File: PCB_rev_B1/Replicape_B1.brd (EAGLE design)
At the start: 107.3 x 69.5 mm, 234 parts, among them IC1 TMC2100-LA, IC10 74AHC1G126DCK, IC11 74AHC1G126DCK, IC12 TMC2100-LA, IC13 74AHC1G126DCK, IC14 74AHC1G126DCK, IC15 TMC2100-LA, IC16 74AHC1G126DCK, IC17 74AHC1G126DCK, IC2 TMC2100-LA, IC3 74AHC1G126DCK, IC4 74AHC1G126DCK, IC5 TMC2100-LA, IC6 74AHC1G126DCK, IC7 74AHC1G126DCK, IC8 74AHC1G126DCK, IC9 74AHC1G126DCK, P8 F-2X23-, P9 F-2X23-, Q1 AON6758, Q2 AON6758, Q3 AON6758, U1 SN74AHC595PW, U10 RT8268, U11 PCA9685PW, U18 CAT24C256, U19 CD4050BD, U2 SN74AHC595PW, U3 SN74AHC595PW, U4 SN74AHC595PW, U5 SN74AHC595PW, U6 MCP16321, X1 22-05-7038-03, X10 22-05-7038-03, X11 22-05-7028-02, X12 22-05-7048-04, X13 22-05-7038-03, X14 22-05-7048-04, X15 22-05-7048-04, X16 22-05-7048-04, X17 22-05-7048-04, X18 22-05-7048-04, X19 22-05-7038-03, X2 MSTBA4, X20 MSTBA4, X21 MSTBA2, X22 22-05-7038-03, X23 22-05-7038-03, X3 MSTBA2, X4 22-05-7028-02, X5 22-05-7028-02, X6 22-05-7028-02, X7 22-05-7028-02, X8 22-05-7028-02, X9 22-05-7028-02

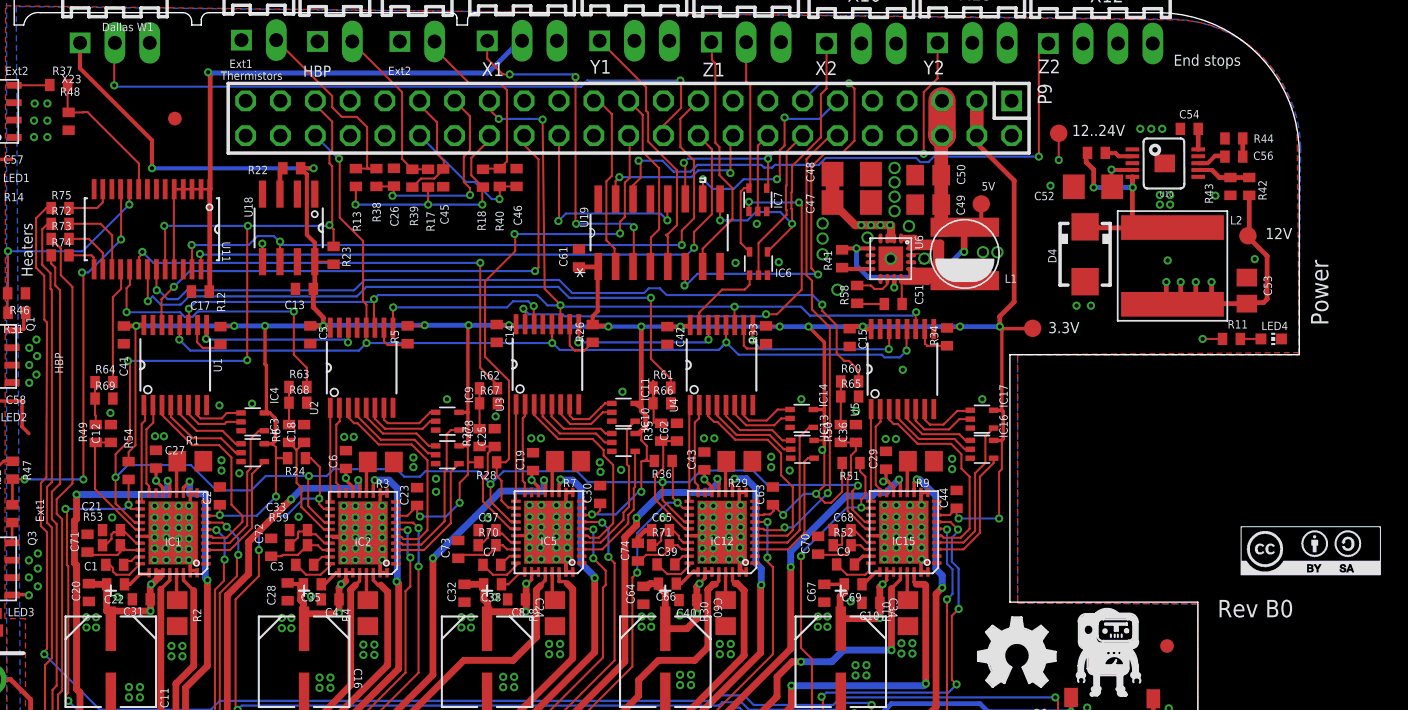
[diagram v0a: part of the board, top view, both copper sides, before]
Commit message: Fixed thermals
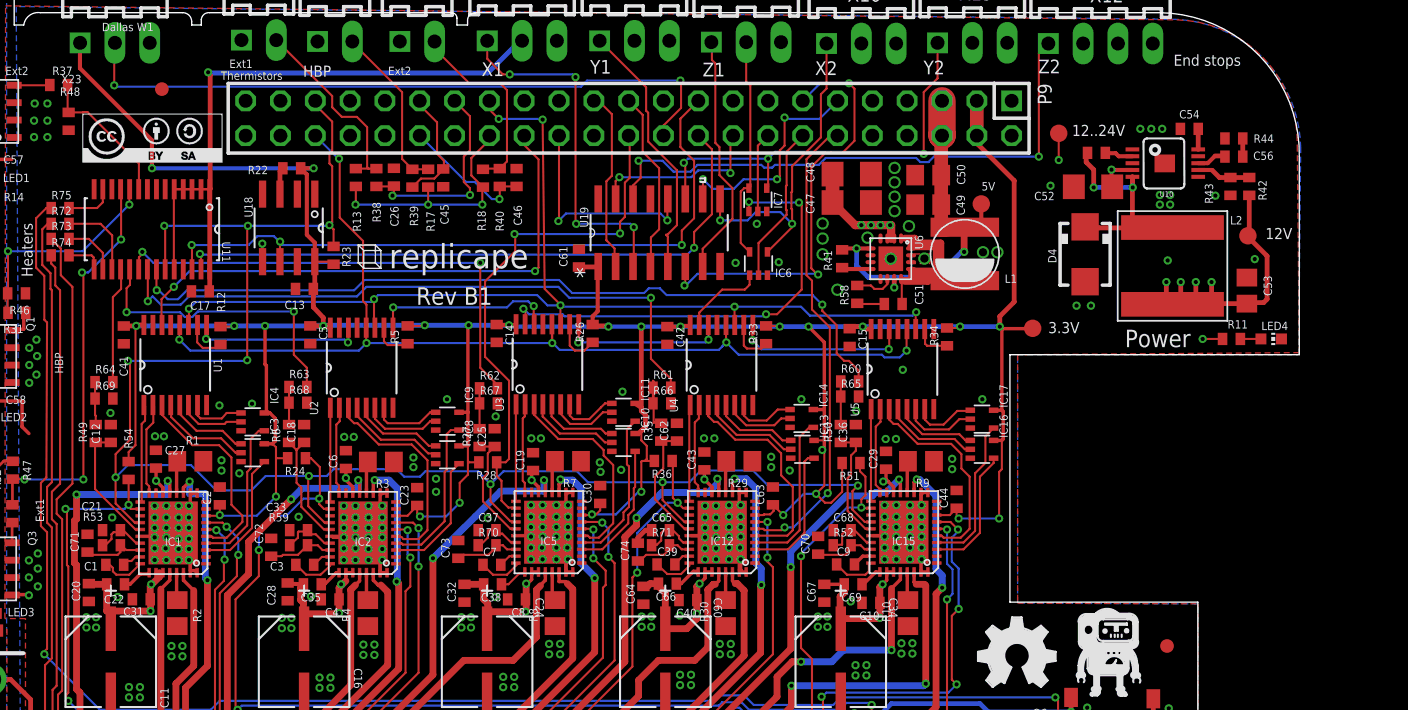
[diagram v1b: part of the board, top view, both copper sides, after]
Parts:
- moved U$3 89.7 mm to (23.8, 58.0)
- moved JP1 2.35 mm to (24.3, 61.1)
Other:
- board text added: "Rev B1"
- board text added: "replicape"
- board text removed: "Rev B0"

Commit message: Added eagleup
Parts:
- removed R31, R32, R37, R72, R73, R74, R75: 470R, rcl:R0402
- moved 12..24V 2.02 mm to (91.0, 59.5)
- moved U$1 0.75 mm to (93.7, 20.0)
- moved C59 0.60 mm to (12.4, 30.4)
- moved D1 0.50 mm to (9.62, 31.7)
- moved X15 0.35 mm to (31.2, 5.40)
- moved X5 0.35 mm to (89.4, 5.40)
- moved X6 0.30 mm to (96.4, 5.40)
- moved C10 0.25 mm to (76.0, 23.9)
- moved X4 0.25 mm to (82.2, 5.40)
- moved X18 0.22 mm to (63.9, 5.40)
- moved X9 0.20 mm to (75.1, 5.40)
- moved C35 0.20 mm to (35.1, 25.0)
- moved X16 0.15 mm to (42.0, 5.40)
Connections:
- removed net FAN_0: Q6.1, R75.1
- removed net FAN_1: Q7.1, R74.1
- removed net FAN_2: Q4.1, R73.1
- removed net FAN_3: Q5.1, R72.1
- removed net N$133: Q3.4, R32.1
- removed net N$23: Q2.4, R37.1
- removed net N$60: Q1.4, R31.1
- net FAN0: now also Q6.1; no longer R75.2
- net FAN1: now also Q7.1; no longer R74.2
- net FAN2: now also Q4.1; no longer R73.2
- net FAN3: now also Q5.1; no longer R72.2
- net HEATER_EXT1: now also Q3.4; no longer R32.2
- net HEATER_EXT2: now also Q2.4; no longer R37.2
- net HEATER_HBP: now also Q1.4; no longer R31.2
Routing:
- net FAN_3: track 121.7 -> 0.00 mm, vias 2 -> 0
- net FAN_1: track 117.4 -> 0.00 mm, vias 2 -> 0
- net FAN1: track 2.75 -> 119.7 mm, vias 0 -> 4
- net FAN3: track 5.98 -> 122.7 mm, vias 0 -> 4
- net FAN_2: track 115.0 -> 0.00 mm, vias 2 -> 0
- net FAN0: track 3.59 -> 117.6 mm, vias 0 -> 4
- net FAN_0: track 112.6 -> 0.00 mm, vias 2 -> 0
- net FAN2: track 4.09 -> 115.2 mm, vias 0 -> 4
- net IREF_E: track 6.42 -> 2.85 mm
- net HEATER_EXT2: track 10.6 -> 14.1 mm
- net HEATER_EXT1: track 29.7 -> 32.5 mm
- net N$60: track 2.81 -> 0.00 mm
- net N$23: track 2.61 -> 0.00 mm
- net N$133: track 1.48 -> 0.00 mm
- net HEATER_HBP: track 15.9 -> 17.3 mm
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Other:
- outline, holes or cut-outs redrawn
- board text added: "12V"
- board text added: "5V"
- board text added: "D"
- board text added: "E"
- board text added: "GND"
- board text added: "H"
- board text removed: "E0"
- board text removed: "E1"
- board text removed: "Ext1"
- board text removed: "Ext2"

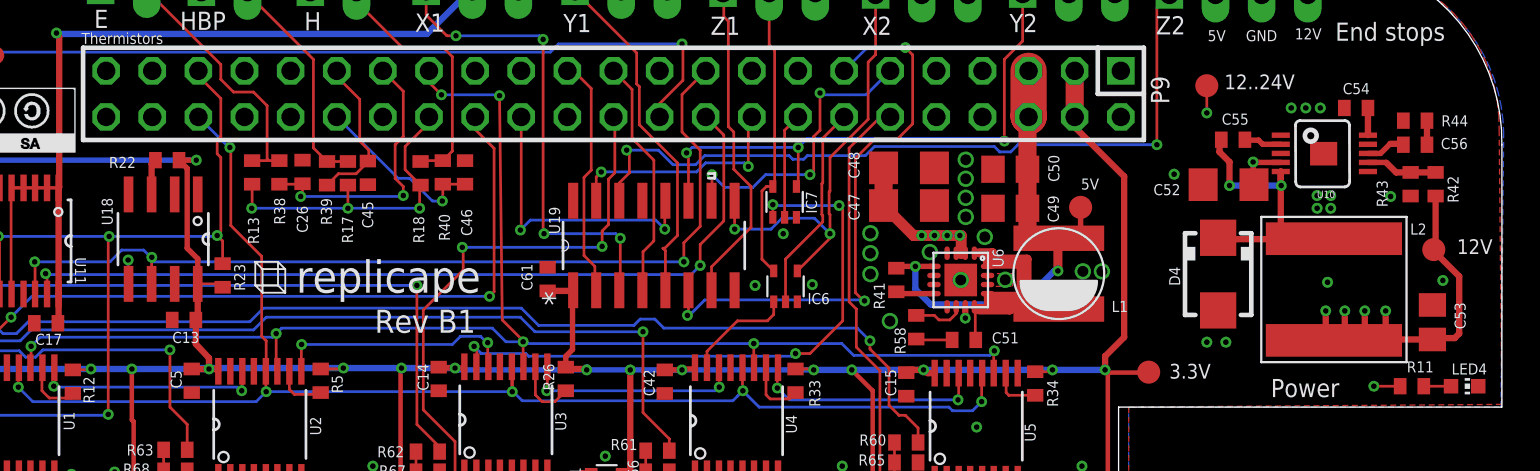
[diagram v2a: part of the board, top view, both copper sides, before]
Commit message: Added EEPROM for developer edition
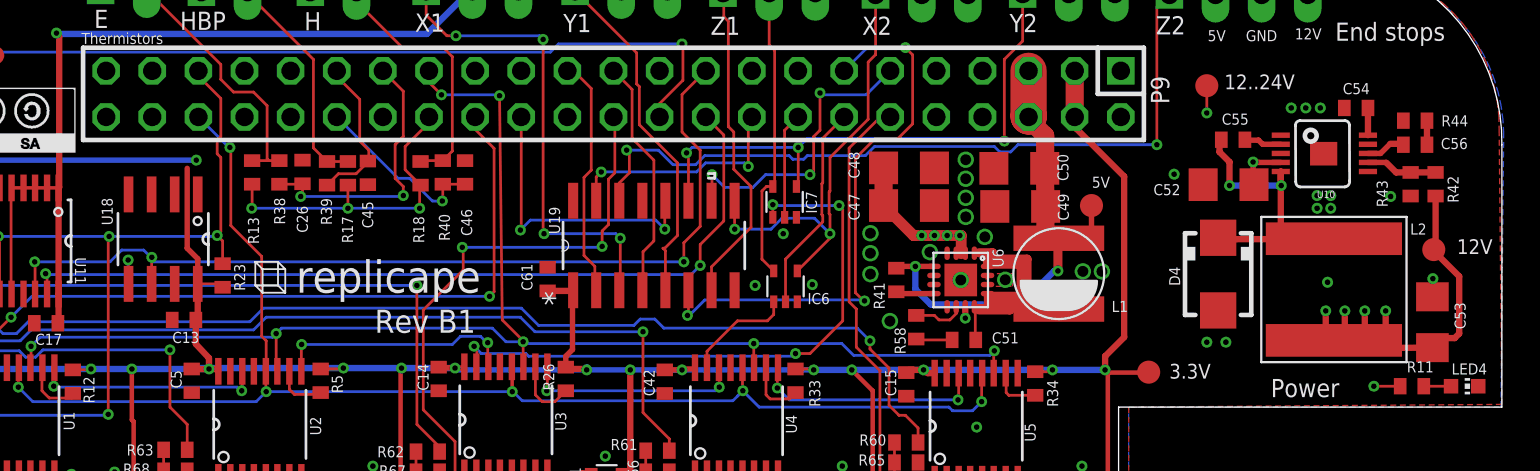
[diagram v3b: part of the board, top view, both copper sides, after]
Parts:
- removed R22: 4.7K, rcl:R0402
- C49, C50: device rcl:C0805 -> rcl:C1206
- C53: value 22uF -> 10uF; device rcl:C0805 -> rcl:C1206
- moved 5V 0.61 mm to (84.7, 52.9)
- moved C49 0.56 mm to (80.8, 52.8)
- moved C50 0.50 mm to (80.7, 54.9)
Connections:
- net N$244 renamed COMP
- removed net N$149: R22.1, U18.3
- net +3V3: now also U18.3; no longer R22.2
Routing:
- net VDD_5V: track 28.9 -> 31.0 mm
- net N$149: track 1.97 -> 0.00 mm
- net +3V3: track 264.5 -> 262.9 mm
- net VDD_12V: track 32.2 -> 33.1 mm
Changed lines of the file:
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@@
 <attribute name="SUPPLIER" value="NXP" x="23.6" y="50.9" size="1.778" layer="27" rot="R270" display="off"/>
 </element>
-<element name="R22" library="rcl" package="R0402" value="4.7K" x="33.8" y="55.35" smashed="yes">
-<attribute name="NAME" x="30.59" y="54.92" size="0.6096" layer="25"/>
-</element>
 <element name="C13" library="rcl" package="C0402" value="0.1uF" x="34.725" y="46.55" smashed="yes" rot="R180">
 <attribute name="NAME" x="35.56" y="45.89" size="0.6096" layer="25" rot="R180"/>
@@
 <attribute name="NAME" x="71.32" y="55.82" size="0.6096" layer="25" rot="R270"/>
 </element>
-<element name="C49" library="rcl" package="C0805" value="22uF" x="80.225" y="52.7" smashed="yes" rot="R180">
-<attribute name="NAME" x="82.293" y="53.4066" size="0.6096" layer="25" rot="R270"/>
+<element name="C49" library="rcl" package="C1206" value="22uF" x="80.775" y="52.8" smashed="yes" rot="R180">
+<attribute name="NAME" x="82.843" y="53.5066" size="0.6096" layer="25" rot="R270"/>
 </element>
-<element name="C50" library="rcl" package="C0805" value="22uF" x="80.225" y="54.85" smashed="yes" rot="R180">
-<attribute name="NAME" x="82.93" y="54.155" size="0.6096" layer="25" rot="R90"/>
+<element name="C50" library="rcl" package="C1206" value="22uF" x="80.725" y="54.9" smashed="yes" rot="R180">
+<attribute name="NAME" x="83.43" y="54.205" size="0.6096" layer="25" rot="R90"/>
 </element>
 <element name="C51" library="rcl" package="C0402" value="22nF" x="77.675" y="45.45" smashed="yes">
@@
 <attribute name="NAME" x="89.595" y="54.03" size="0.6096" layer="25" rot="R180"/>
 </element>
-<element name="C53" library="rcl" package="C0805" value="22uF" x="103.475" y="46.425" smashed="yes" rot="R90">
+<element name="C53" library="rcl" package="C1206" value="10uF" x="103.475" y="46.425" smashed="yes" rot="R90">
 <attribute name="NAME" x="104.695" y="47.52" size="0.6096" layer="25" rot="R270"/>
 </element>
@@
 <attribute name="TP_SIGNAL_NAME" value="" x="102.915" y="48.52" size="1" layer="37"/>
 </element>
-<element name="5V" library="testpad" package="B1,27" value="TPB1,27" x="84.1" y="52.75" smashed="yes" rot="R270">
-<attribute name="NAME" x="84.123" y="53.731" size="0.6096" layer="25" ratio="10"/>
-<attribute name="TP_SIGNAL_NAME" value="" x="82.195" y="53.385" size="1" layer="37" rot="R270"/>
+<element name="5V" library="testpad" package="B1,27" value="TPB1,27" x="84.7" y="52.85" smashed="yes" rot="R270">
+<attribute name="NAME" x="84.723" y="53.831" size="0.6096" layer="25" ratio="10"/>
+<attribute name="TP_SIGNAL_NAME" value="" x="82.795" y="53.485" size="1" layer="37" rot="R270"/>
 </element>
 <element name="12..24V" library="testpad" package="B1,27" value="TPB1,27" x="91.05" y="59.45" smashed="yes">
@@
 <via x="91.05" y="45.325" extent="1-16" drill="0.305"/>
 <via x="28.525" y="38.05" extent="1-16" drill="0.305"/>
-<via x="104.05" y="48.725" extent="1-16" drill="0.305"/>
+<via x="103.5" y="48.825" extent="1-16" drill="0.305"/>
 <via x="97.7" y="48.625" extent="1-16" drill="0.305"/>
 <via x="97.125" y="53.4" extent="1-16" drill="0.305"/>
@@
 <contactref element="D5" pad="A"/>
 <polygon width="0.4064" layer="2" thermals="no">
-<vertex x="-0.4" y="69.75"/>
-<vertex x="111" y="69.75"/>
-<vertex x="111" y="-3.3"/>
-<vertex x="-0.4" y="-3.3"/>
+<vertex x="-0.45" y="69.55"/>
+<vertex x="107.25" y="69.8"/>
+<vertex x="107.1" y="0.2"/>
+<vertex x="-0.6" y="-0.05"/>
 </polygon>
 <via x="23.8" y="30.675" extent="1-16" drill="0.305" shape="square"/>
@@
 <wire x1="104.95" y1="45.8" x2="104.7" y2="45.55" width="0.35" layer="1"/>
 <wire x1="104.7" y1="45.55" x2="103.55" y2="45.55" width="0.35" layer="1"/>
-<wire x1="103.55" y1="45.55" x2="103.475" y2="45.475" width="0.35" layer="1"/>
+<wire x1="103.55" y1="45.55" x2="103.475" y2="45.025" width="0.35" layer="1"/>
 <contactref element="X4" pad="1"/>
 <contactref element="R19" pad="2"/>
@@
 <vertex x="71" y="3.4"/>
 </polygon>
-<wire x1="103.475" y1="45.475" x2="98.1" y2="45.475" width="0.35" layer="1"/>
+<wire x1="103.475" y1="45.025" x2="99.45" y2="45" width="0.35" layer="1"/>
+<wire x1="99.45" y1="45" x2="99.45" y2="45.475" width="0.35" layer="1"/>
+<wire x1="99.45" y1="45.475" x2="98.1" y2="45.475" width="0.35" layer="1"/>
 <wire x1="98.1" y1="45.475" x2="98.05" y2="45.425" width="0.35" layer="1"/>
 <wire x1="98.05" y1="45.425" x2="100.9" y2="45.425" width="0.35" layer="1"/>
@@
 <wire x1="56.7" y1="24.95" x2="56.7" y2="26" width="0.1524" layer="1"/>
 </signal>
-<signal name="N$149">
-<contactref element="R22" pad="1"/>
-<contactref element="U18" pad="3"/>
-<wire x1="32.94" y1="53.4638" x2="32.94" y2="55.14" width="0.35" layer="1"/>
-<wire x1="32.94" y1="55.14" x2="33.15" y2="55.35" width="0.35" layer="1"/>
-</signal>
 <signal name="N$9">
 <contactref element="LED5" pad="A"/>
@@
 </signal>
 <signal name="+3V3">
-<contactref element="R22" pad="2"/>
 <contactref element="C13" pad="1"/>
 <contactref element="U1" pad="16"/>
@@
 <wire x1="35.48" y1="49.92" x2="34.9" y2="50.5" width="0.3" layer="1"/>
 <wire x1="34.9" y1="50.5" x2="34.9" y2="54.9" width="0.3" layer="1"/>
-<wire x1="34.9" y1="54.9" x2="34.45" y2="55.35" width="0.3" layer="1"/>
 <contactref element="IC1" pad="8"/>
 <contactref element="C2" pad="1"/>
@@
 <wire x1="28.65" y1="30" x2="31.25" y2="30" width="0.1524" layer="16"/>
 <wire x1="49.65" y1="43.9" x2="49.621" y2="43.9" width="0.1524" layer="16"/>
-<wire x1="34.45" y1="55.35" x2="35.4" y2="55.35" width="0.3" layer="1"/>
 <via x="35.4" y="55.35" extent="1-16" drill="0.3"/>
 <wire x1="35.4" y1="55.35" x2="23.6" y2="55.35" width="0.3" layer="16"/>
@@
 <wire x1="50.093" y1="43.9" x2="49.65" y2="43.9" width="0.3" layer="1"/>
 <wire x1="49.6" y1="43.9" x2="49.65" y2="43.9" width="0.3" layer="1"/>
+<contactref element="U18" pad="3"/>
+<wire x1="34.9" y1="54.9" x2="32.94" y2="53.4638" width="0" layer="19" extent="1-1"/>
+<wire x1="35.4" y1="55.35" x2="34.9" y2="54.9" width="0" layer="19" extent="1-1"/>
 </signal>
 <signal name="N$96">
@@
 <contactref element="P9" pad="6"/>
 <wire x1="81.25" y1="57.75" x2="81.235" y2="57.73" width="0.1524" layer="1"/>
-<wire x1="81.175" y1="54.85" x2="81.175" y2="52.7" width="1" layer="1"/>
-<wire x1="81.175" y1="52.7" x2="81.175" y2="50.85" width="1" layer="1"/>
+<wire x1="82.125" y1="54.9" x2="82.175" y2="52.8" width="1" layer="1"/>
+<wire x1="82.175" y1="52.8" x2="82.15" y2="50.95" width="1" layer="1"/>
+<wire x1="82.15" y1="50.95" x2="82.15" y2="50.85" width="1" layer="1"/>
+<wire x1="82.15" y1="50.85" x2="81.45" y2="50.85" width="1" layer="1"/>
 <wire x1="81.175" y1="50.85" x2="81.45" y2="50.85" width="1" layer="1"/>
 <wire x1="81.45" y1="50.85" x2="82.9" y2="51.05" width="1" layer="1"/>
@@
 <wire x1="81.25" y1="57.75" x2="81.235" y2="57.765" width="2" layer="1"/>
 <wire x1="81.235" y1="57.765" x2="81.235" y2="60.27" width="2" layer="1"/>
-<wire x1="81.175" y1="54.85" x2="81.175" y2="57.67" width="1" layer="1"/>
+<wire x1="82.125" y1="54.9" x2="82.15" y2="54.9" width="1" layer="1"/>
+<wire x1="82.15" y1="54.9" x2="82.15" y2="56.7" width="1" layer="1"/>
+<wire x1="82.15" y1="56.7" x2="81.175" y2="57.67" width="1" layer="1"/>
 <wire x1="81.175" y1="57.67" x2="81.235" y2="57.73" width="1" layer="1"/>
 <wire x1="82.85" y1="49.25" x2="82.65" y2="49.25" width="0.35" layer="16"/>
@@
 <wire x1="76" y1="49.5" x2="75" y2="49.5" width="0.3" layer="1"/>
 <wire x1="74.05" y1="49.5" x2="75" y2="49.5" width="0.3" layer="1"/>
-<wire x1="84.1" y1="52.75" x2="84.1" y2="51.35" width="0.3" layer="1"/>
-<wire x1="84.1" y1="51.35" x2="83.7" y2="50.95" width="0.3" layer="1"/>
-<wire x1="83.7" y1="50.95" x2="82.95" y2="50.95" width="0.3" layer="1"/>
+<wire x1="84.7" y1="52.85" x2="84.7" y2="50.95" width="0.3" layer="1"/>
+<wire x1="84.7" y1="50.95" x2="82.95" y2="50.95" width="0.3" layer="1"/>
 <wire x1="82.95" y1="50.95" x2="82.9" y2="51.05" width="0.3" layer="1"/>
 <wire x1="81.175" y1="57.67" x2="81.175" y2="57.625" width="0.3" layer="1"/>
@@
 <wire x1="93.175" y1="56.45" x2="93.15" y2="56.475" width="0.3" layer="1"/>
 </signal>
-<signal name="N$244">
+<signal name="COMP">
 <contactref element="U10" pad="8"/>
 <contactref element="C56" pad="1"/>
